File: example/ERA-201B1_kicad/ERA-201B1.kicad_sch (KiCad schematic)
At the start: 115 parts, among them CN1 Conn_01x02, CN2 Conn_01x01, CN3 Conn_01x01, CN4 Conn_01x01, CN5 Conn_01x06, IC1 S-8232AAFT, IC200 TLV70433DBVR, IC21 PS302F-I_SN, IC41 BQ2040SN-C408, IC42 24LC01B-I_SN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

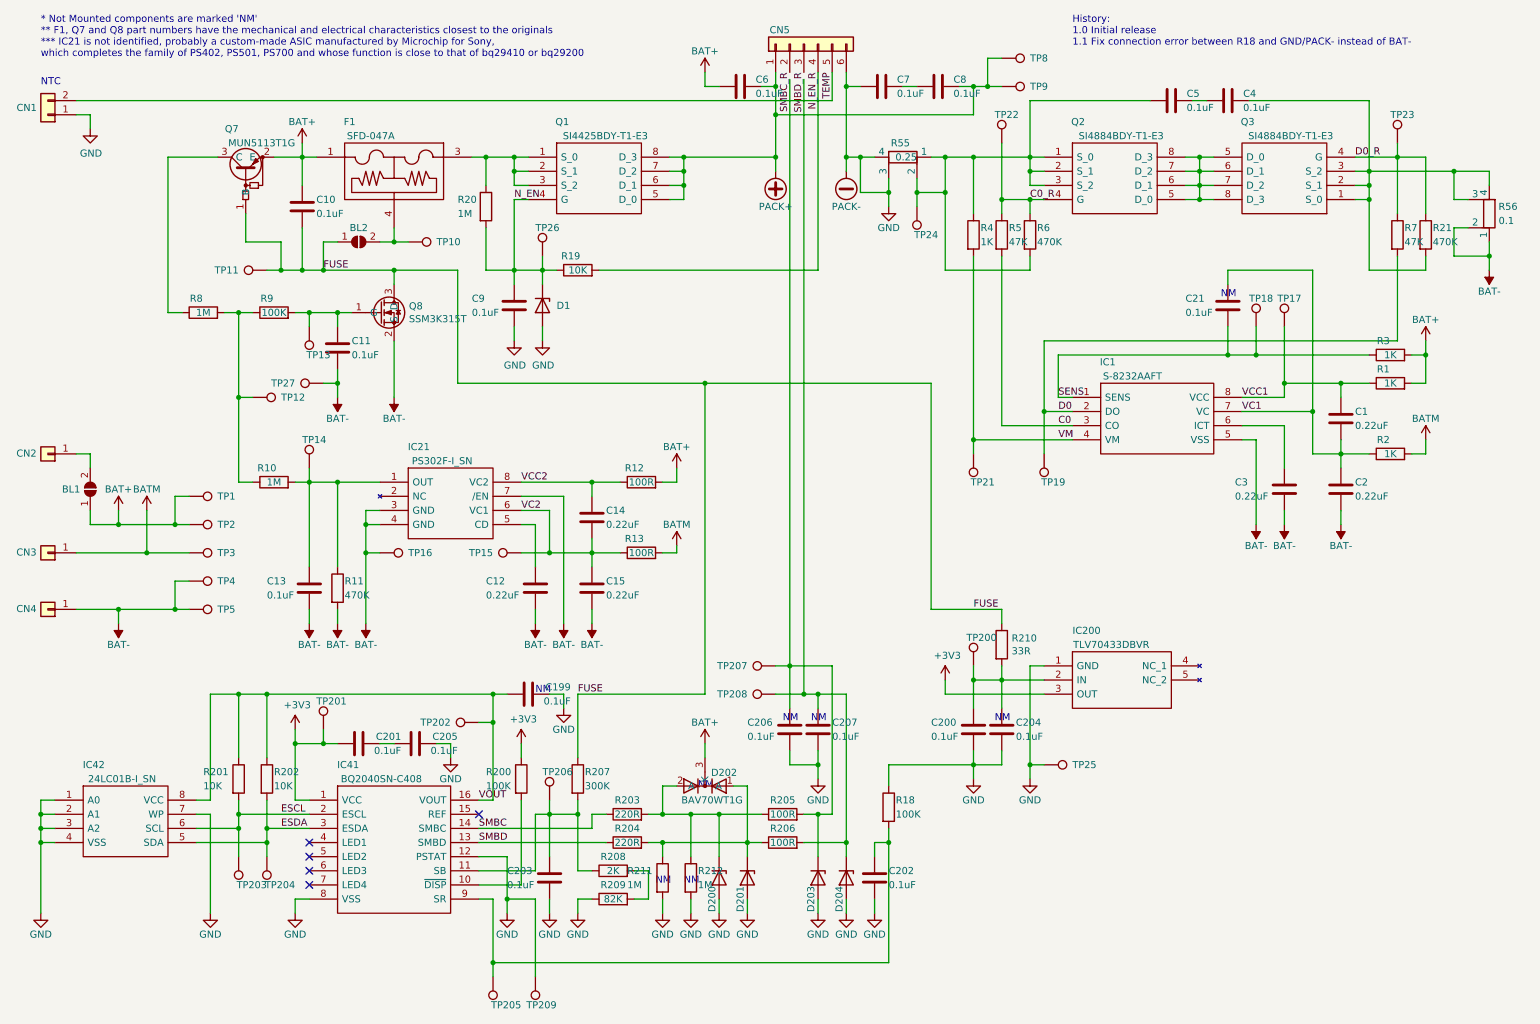
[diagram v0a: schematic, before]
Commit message: Release version 1.2 of the ERA-201B1 reverse engineering schematic
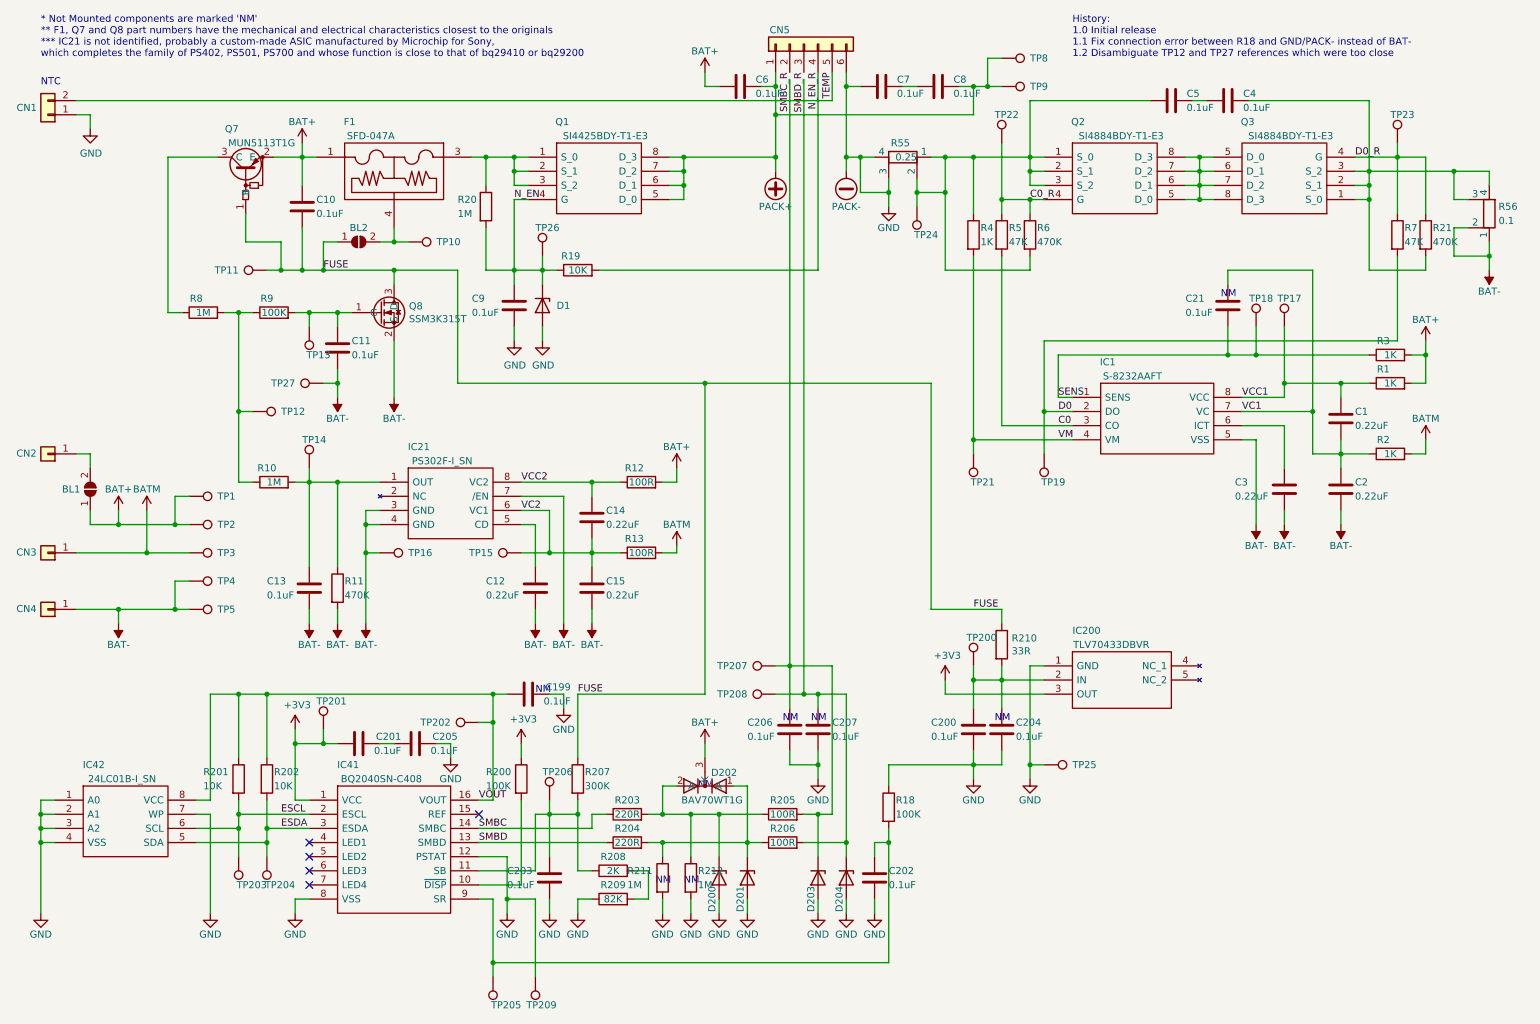
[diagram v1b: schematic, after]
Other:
- note added: "History: 1.0 Initial release 1.1 Fix connection error between R18 and GND/PACK- instead of BAT- 1.2 Disambiguate TP12 and TP27 references which were too close"
- note removed: "History: 1.0 Initial release 1.1 Fix connection error between R18 and GND/PACK- instead of BAT-"
- moved on the sheet: TP12
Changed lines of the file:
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@@
   (title_block
     (title "ERA-201B1 reverse engineering schematic")
-    (date "2022-02-26")
-    (rev "1.1")
+    (date "2022-04-27")
+    (rev "1.2")
     (company "Loïc POLLIER")
     (comment 3 "for Aibo ERS-210 and ERS-220 robots")
@@
   (junction (at 31.75 121.92) (diameter 0) (color 0 0 0 0)
   )
-  (junction (at 53.34 83.82) (diameter 0) (color 0 0 0 0)
+  (junction (at 53.34 86.36) (diameter 0) (color 0 0 0 0)
   )
   (junction (at 157.48 137.16) (diameter 0) (color 0 0 0 0)
@@
     (stroke (width 0) (type default) (color 0 0 0 0))
   )
-  (wire (pts (xy 55.88 83.82) (xy 53.34 83.82))
+  (wire (pts (xy 55.88 86.36) (xy 53.34 86.36))
     (stroke (width 0) (type default) (color 0 0 0 0))
   )
@@
     (stroke (width 0) (type default) (color 0 0 0 0))
   )
-  (wire (pts (xy 53.34 68.58) (xy 53.34 83.82))
-    (stroke (width 0) (type default) (color 0 0 0 0))
-  )
   (wire (pts (xy 256.54 30.48) (xy 256.54 43.18))
     (stroke (width 0) (type default) (color 0 0 0 0))
@@
     (stroke (width 0) (type default) (color 0 0 0 0))
   )
+  (wire (pts (xy 53.34 86.36) (xy 53.34 99.06))
+    (stroke (width 0) (type default) (color 0 0 0 0))
+  )
   (wire (pts (xy 256.54 48.26) (xy 256.54 60.96))
     (stroke (width 0) (type default) (color 0 0 0 0))
@@
     (stroke (width 0) (type default) (color 0 0 0 0))
   )
-  (wire (pts (xy 53.34 83.82) (xy 53.34 99.06))
+  (wire (pts (xy 53.34 68.58) (xy 53.34 86.36))
     (stroke (width 0) (type default) (color 0 0 0 0))
   )
@@
     (effects (font (size 1.27 1.27)) (justify left bottom))
   )
-  (text "History:\n1.0 Initial release\n1.1 Fix connection error between R18 and GND/PACK- instead of BAT-\n "
+  (text "History:\n1.0 Initial release\n1.1 Fix connection error between R18 and GND/PACK- instead of BAT-\n1.2 Disambiguate TP12 and TP27 references which were too close"
     (at 203.2 22.86 0)
     (effects (font (size 1.27 1.27)) (justify left bottom))
@@
     (pin "1")
   )
-  (symbol (lib_id "Connector:TestPoint") (at 55.88 83.82 270) (unit 1)
+  (symbol (lib_id "Connector:TestPoint") (at 55.88 86.36 270) (unit 1)
     (in_bom yes) (on_board yes)
-    (property "Reference" "TP12" (id 0) (at 60.96 83.82 90)
+    (property "Reference" "TP12" (id 0) (at 60.96 86.36 90)
       (effects (font (size 1.27 1.27)) (justify left))
     )
-    (property "Value" "TestPoint" (id 1) (at 56.5658 85.2932 0)
+    (property "Value" "TestPoint" (id 1) (at 56.5658 87.8332 0)
       (effects (font (size 1.27 1.27)) (justify left) hide)
     )
-    (property "Footprint" "" (id 2) (at 55.88 88.9 0)
+    (property "Footprint" "" (id 2) (at 55.88 91.44 0)
       (effects (font (size 1.27 1.27)) hide)
     )
-    (property "Datasheet" "~" (id 3) (at 55.88 88.9 0)
+    (property "Datasheet" "~" (id 3) (at 55.88 91.44 0)
       (effects (font (size 1.27 1.27)) hide)
     )

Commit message: Release version 1.3 of the ERA-201B1 reverse engineering schematic
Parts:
- removed IC21: PS302F-I_SN, SOIC127P600X175-8N, symbol PS302F-I_SN:PS302F-I_SN
- added IC21: MM1302F, SOIC127P600X175-8N, symbol MM1302F:MM1302F
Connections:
- net -BATT: now also IC21.3 (DS), IC21.4 (GND), IC21.7 (CS)
- net VC2: now also IC21.6 (VL)
- net VCC2: now also IC21.8 (VH)
- net at C13.1, R10.2, R11.1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: now also IC21.1 (OC)
- net at C12.1: now also IC21.5 (TD)
- no-connect marks 5 -> 6
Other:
- note added: "* Not Mounted components are marked 'NM' ** F1, Q7 and Q8 part numbers have the mechanical and electrical characteristics closest to the originals *** IC21 is identified as Mitsumi MM1302F, a 2 cell Li-ion battery overvoltage protection"
- note added: "History: 1.0 Initial release 1.1 Fix connection error between R18 and GND/PACK- instead of BAT- 1.2 Disambiguate TP12 and TP27 references which were too close 1.3 Replace IC21 part number from PS302F-I_SN to MM1302F"
- note removed: "* Not Mounted components are marked 'NM' ** F1, Q7 and Q8 part numbers have the mechanical and electrical characteristics closest to the originals *** IC21 is not identified, probably a custom-made ASIC manufactured by Microchip for Sony, which completes the family of PS402, PS501, PS700 and whose function is close to that of bq29410 or bq29200"
- note removed: "History: 1.0 Initial release 1.1 Fix connection error between R18 and GND/PACK- instead of BAT- 1.2 Disambiguate TP12 and TP27 references which were too close"
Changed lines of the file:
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@@
   (title_block
     (title "ERA-201B1 reverse engineering schematic")
-    (date "2022-04-27")
-    (rev "1.2")
+    (date "2022-09-27")
+    (rev "1.3")
     (company "Loïc POLLIER")
     (comment 3 "for Aibo ERS-210 and ERS-220 robots")
-    (comment 4 "Sony Lithium-Ion Battery Pack (ERA-201B1) reverse engineering schematic")
+    (comment 4 "Sony Lithium-ion Battery Pack (ERA-201B1) reverse engineering schematic")
   )
   (junction (at 36.83 111.76) (diameter 0) (color 0 0 0 0)
@@
   (no_connect (at 66.04 166.37))
   (no_connect (at 66.04 163.83))
+  (no_connect (at 78.74 101.6))
   (wire (pts (xy 44.45 101.6) (xy 41.91 101.6))
     (stroke (width 0) (type default) (color 0 0 0 0))
@@
     (effects (font (size 1.27 1.27)) (justify left bottom))
   )
-  (text "* Not Mounted components are marked 'NM'\n** F1, Q7 and Q8 part numbers have the mechanical and electrical characteristics closest to the originals\n*** IC21 is not identified, probably a custom-made ASIC manufactured by Microchip for Sony,\nwhich completes the family of PS402, PS501, PS700 and whose function is close to that of bq29410 or bq29200"
-    (at 17.78 22.86 0)
-    (effects (font (size 1.27 1.27)) (justify left bottom))
-  )
   (text "NM" (at 189.23 142.24 0)
     (effects (font (size 1.27 1.27)) (justify left bottom))
@@
     (effects (font (size 1.27 1.27)) (justify left bottom))
   )
+  (text "History:\n1.0 Initial release\n1.1 Fix connection error between R18 and GND/PACK- instead of BAT-\n1.2 Disambiguate TP12 and TP27 references which were too close\n1.3 Replace IC21 part number from PS302F-I_SN to MM1302F\n "
+    (at 203.2 26.924 0)
+    (effects (font (size 1.27 1.27)) (justify left bottom))
+  )
   (text "NM" (at 106.68 137.16 0)
     (effects (font (size 1.27 1.27)) (justify left bottom))
@@
     (effects (font (size 1.27 1.27)) (justify left bottom))
   )
-  (text "History:\n1.0 Initial release\n1.1 Fix connection error between R18 and GND/PACK- instead of BAT-\n1.2 Disambiguate TP12 and TP27 references which were too close"
-    (at 203.2 22.86 0)
+  (text "* Not Mounted components are marked 'NM'\n** F1, Q7 and Q8 part numbers have the mechanical and electrical characteristics closest to the originals\n*** IC21 is identified as Mitsumi MM1302F, a 2 cell Li-ion battery overvoltage protection"
+    (at 17.78 20.828 0)
     (effects (font (size 1.27 1.27)) (justify left bottom))
   )
@@
     (pin "1")
   )
-  (symbol (lib_id "PS302F-I_SN:PS302F-I_SN") (at 78.74 99.06 0) (unit 1)
-    (in_bom yes) (on_board yes)
-    (property "Reference" "IC21" (id 0) (at 85.725 92.71 0))
-    (property "Value" "PS302F-I_SN" (id 1) (at 89.916 95.25 0))
-    (property "Footprint" "SOIC127P600X175-8N" (id 2) (at 100.33 96.52 0)
-      (effects (font (size 1.27 1.27)) (justify left) hide)
-    )
-    (property "Datasheet" "https://ww1.microchip.com/downloads/en/devicedoc/21711c.pdf" (id 3) (at 100.33 83.82 0)
-      (effects (font (size 1.27 1.27)) (justify left) hide)
-    )
-    (property "Description" "Voltage Protection for 2-Series Cell Li-Ion Batteries (2nd level protection), 8-Pin SOIC" (id 4) (at 100.33 88.9 0)
-      (effects (font (size 1.27 1.27)) (justify left) hide)
-    )
-    (property "Manufacturer_Name" "Microchip" (id 5) (at 100.33 86.36 0)
-      (effects (font (size 1.27 1.27)) (justify left) hide)
-    )
-    (pin "1")
-    (pin "2")
-    (pin "3")
-    (pin "4")
-    (pin "5")
-    (pin "6")
-    (pin "7")
-    (pin "8")
-  )
   (symbol (lib_id "power:+BATT") (at 266.7 73.66 0) (unit 1)
     (in_bom yes) (on_board yes)
@@
   (symbol (lib_id "Device:C") (at 109.22 170.18 0) (unit 1)
     (in_bom yes) (on_board yes)
-    (property "Reference" "C203" (id 0) (at 101.6 168.91 0)
+    (property "Reference" "C203" (id 0) (at 111.76 168.91 0)
       (effects (font (size 1.27 1.27)) (justify left))
     )
-    (property "Value" "0.1uF" (id 1) (at 101.6 171.45 0)
+    (property "Value" "0.1uF" (id 1) (at 111.76 171.45 0)
       (effects (font (size 1.27 1.27)) (justify left))
     )
@@
     (pin "1")
   )
+  (symbol (lib_name "MM1302F_1") (lib_id "MM1302F:MM1302F") (at 78.74 99.06 0) (unit 1)
+    (in_bom yes) (on_board yes)
+    (property "Reference" "IC21" (id 0) (at 85.725 92.71 0))
+    (property "Value" "MM1302F" (id 1) (at 88.011 95.25 0))
+    (property "Footprint" "SOIC127P600X175-8N" (id 2) (at 100.33 96.52 0)
+      (effects (font (size 1.27 1.27)) (justify left) hide)
+    )
+    (property "Datasheet" "https://cdn.datasheetspdf.com/pdf-down/M/M/1/MM1302F_MITSUMIELECTRIC.pdf" (id 3) (at 100.33 83.82 0)
+      (effects (font (size 1.27 1.27)) (justify left) hide)
+    )
+    (property "Description" "Voltage Protection for 2-Series Cell Li-Ion Batteries (2nd level protection), 8-Pin SOIC" (id 4) (at 100.33 88.9 0)
+      (effects (font (size 1.27 1.27)) (justify left) hide)
+    )
+    (property "Manufacturer_Name" "Mitsumi" (id 5) (at 100.33 86.36 0)
+      (effects (font (size 1.27 1.27)) (justify left) hide)
+    )
+    (pin "1")
+    (pin "2")
+    (pin "3")
+    (pin "4")
+    (pin "5")
+    (pin "6")
+    (pin "7")
+    (pin "8")
+  )
   (sheet_instances
     (path "/" (page "1"))
@@
       (reference "IC1") (unit 1) (value "S-8232AAFT") (footprint "SOP65P640X120-8N")
     )
-    (path "/00000000-0000-0000-0000-0000605c7100"
-      (reference "IC21") (unit 1) (value "PS302F-I_SN") (footprint "SOIC127P600X175-8N")
+    (path "/e98a0ca0-541d-4c93-b642-ca88fe038b30"
+      (reference "IC21") (unit 1) (value "MM1302F") (footprint "SOIC127P600X175-8N")
     )
     (path "/00000000-0000-0000-0000-00006068aafb"
